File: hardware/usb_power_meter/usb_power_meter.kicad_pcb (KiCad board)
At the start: 4 copper layers, 37.5 x 39.1 mm, 37 parts, among them J1 Conn_ARM_JTAG_SWD_10, J2 917-P81A202ES60201, J4 USB_A, Q1 2N7002, Q2 IRML6401, U1 nRF52833-QDxx, U2 INA226, X1 32Mhz crystal, X2 32.768kHz crystal

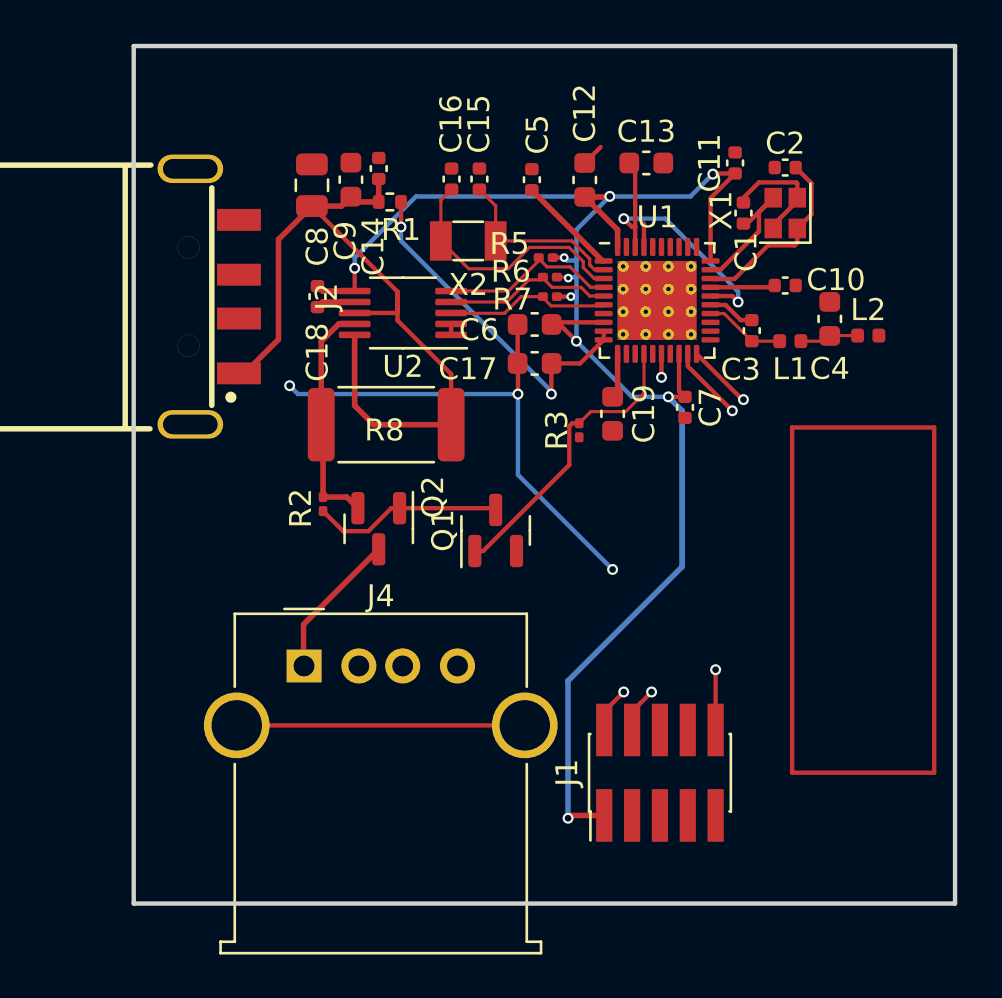
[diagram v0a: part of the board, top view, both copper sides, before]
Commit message: Add an USB socket
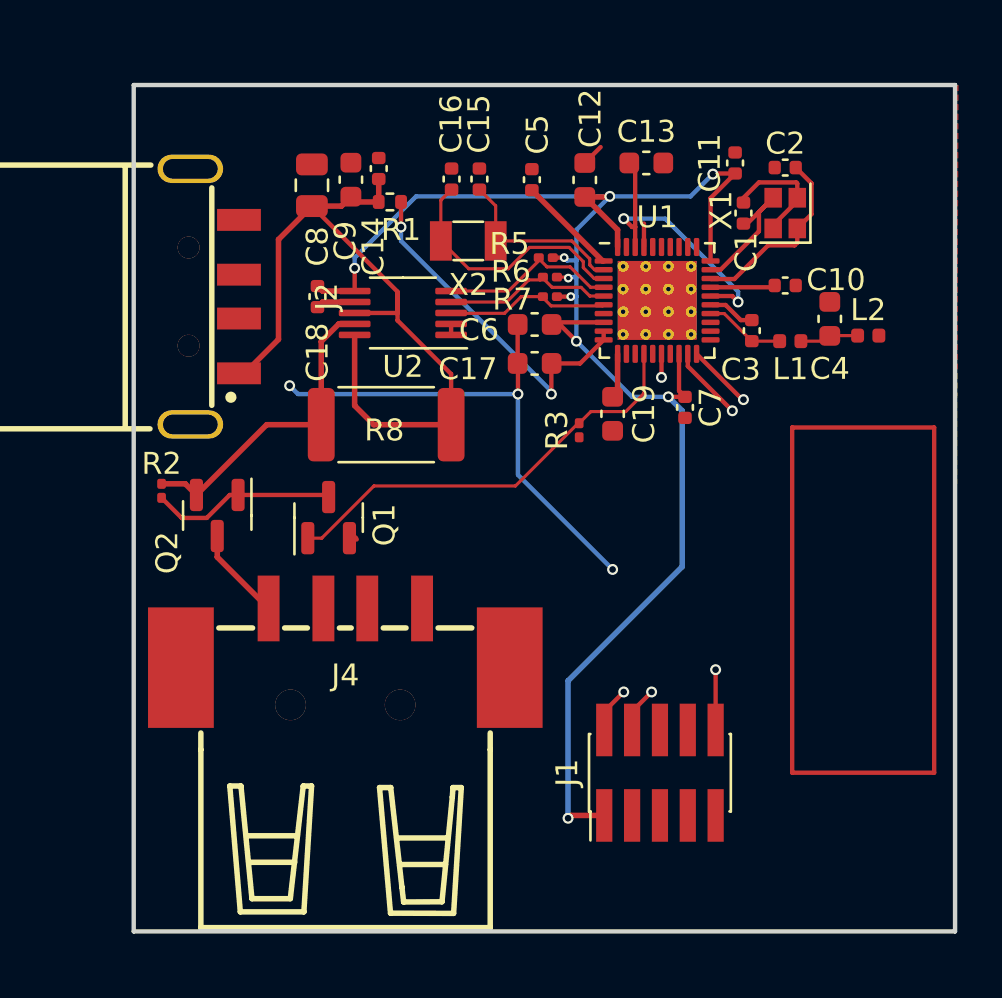
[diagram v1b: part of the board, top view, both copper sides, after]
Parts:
- J4: value USB_A -> A/F LCPTrue color1.2pillar_C42605; footprint Connector_USB:USB_A_Molex_67643_Horizontal -> easyeda2kicad:USB-A-SMD_USB-M-32
- moved Q1 7.64 mm to (119.1, 112.7)
- moved Q2 7.39 mm to (114.0, 112.6)
- moved R2 7.39 mm to (111.5, 111.5)
- moved J4 2.27 mm to (119.9, 118.2)
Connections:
- J4 pad 1: Net-(J4-VBUS) -> GND
- J4 pad 4: GND -> Net-(J4-VCC)
- Q2 pad 3: Net-(J4-VBUS) -> Net-(J4-VCC)
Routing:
- net unconnected-(J4-Pad5): track 13.1 -> 0.00 mm
- net Net-(J4-VBUS): track 6.75 -> 0.00 mm
- net /EN_PWR: track 13.5 -> 19.9 mm
- net Net-(J4-VCC): track 0.00 -> 4.27 mm
- net Net-(Q2-S): track 10.8 -> 14.5 mm
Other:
- board size 37.5 x 39.1 mm -> 37.5 x 38.6 mm

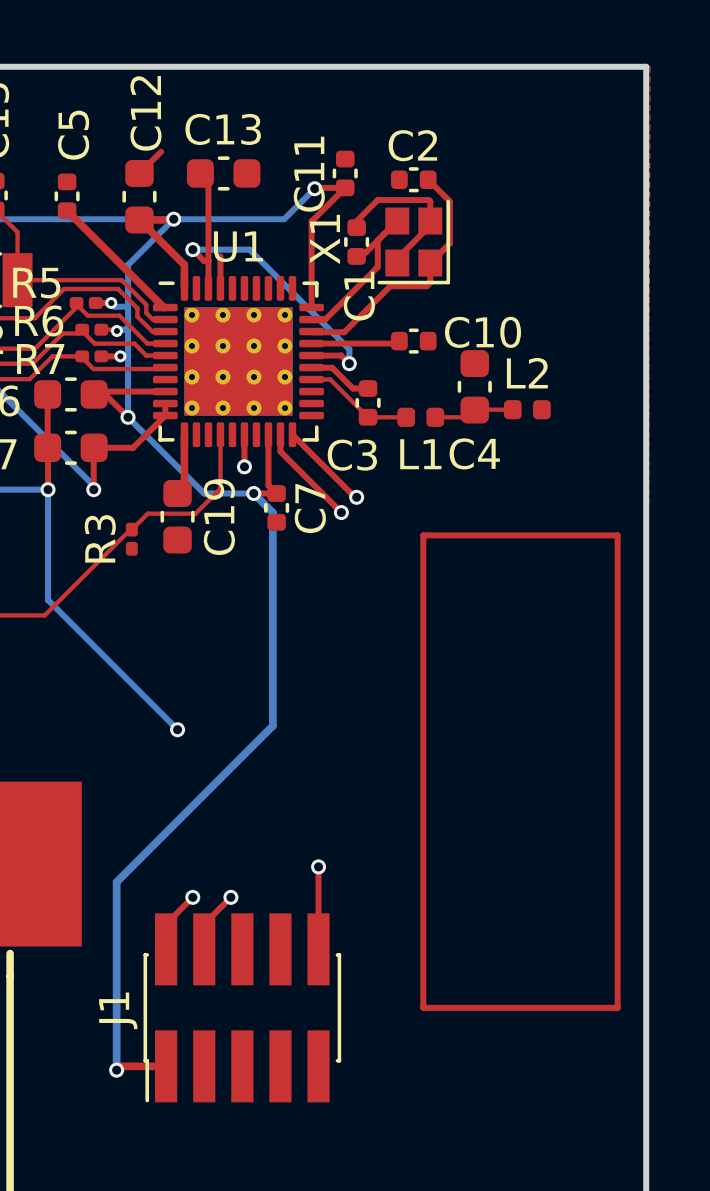
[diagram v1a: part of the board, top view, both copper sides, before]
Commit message: Add the antenna
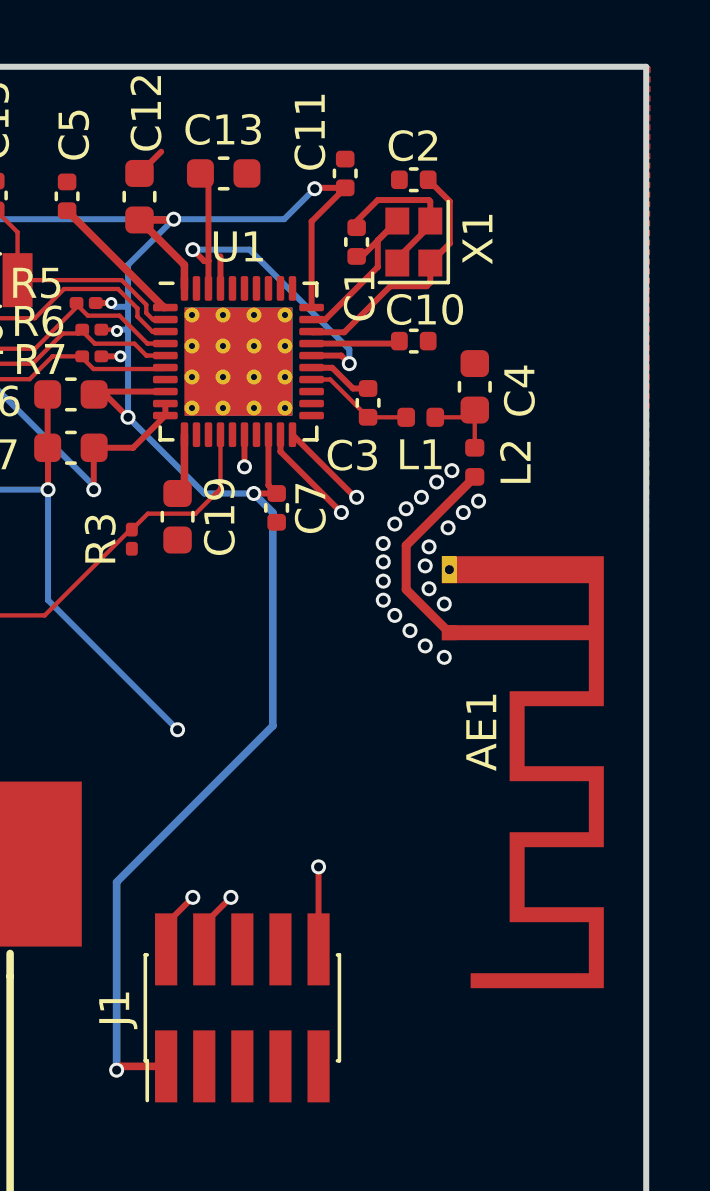
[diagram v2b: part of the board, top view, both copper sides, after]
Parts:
- added AE1: Antenna, RF_Antenna:Texas_SWRA117D_2.4GHz_Right, F.Cu at (141.1, 111.8)
- moved L2 2.48 mm to (142.0, 106.1), turned to -90 degrees
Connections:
- L2 pad 2: unconnected-(L2-Pad2) -> Net-(AE1-A)
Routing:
- net Net-(AE1-A): track 0.00 -> 6.74 mm
- net GND: vias 3 -> 23
- added copper zone on In1.Cu, net GND

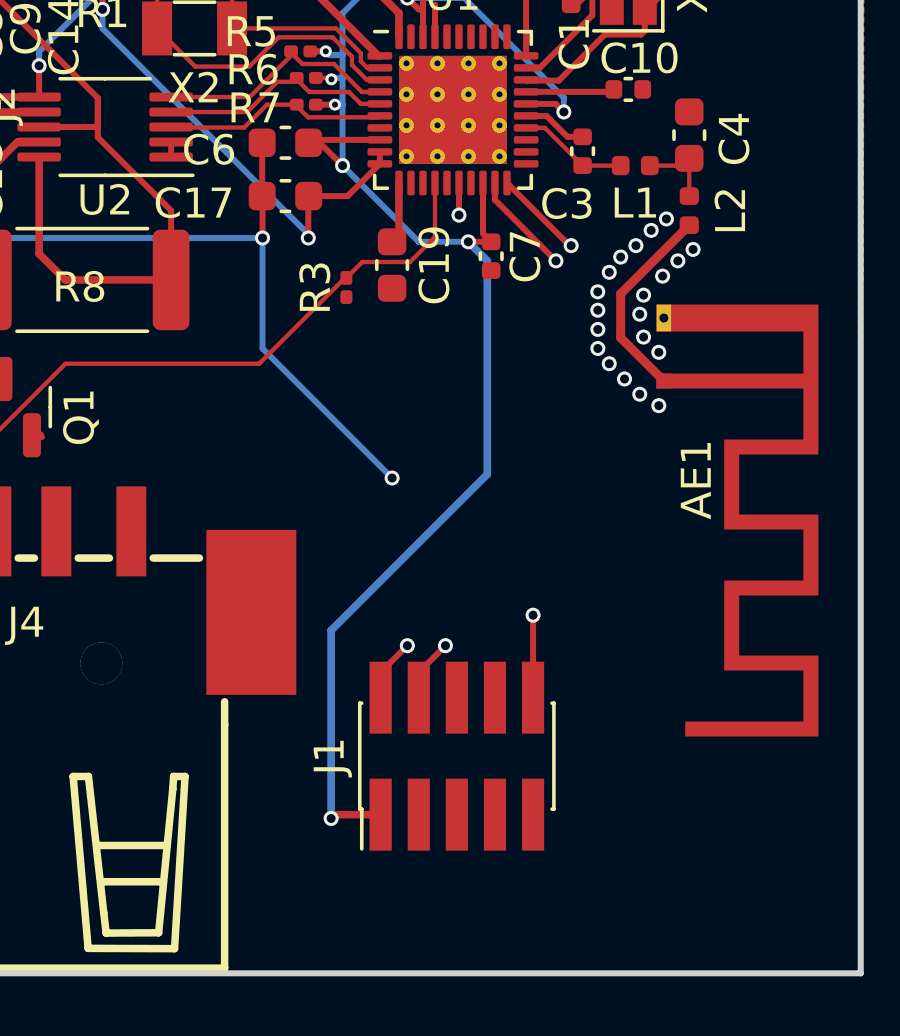
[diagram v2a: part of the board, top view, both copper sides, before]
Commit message: Add and route debugging connectors
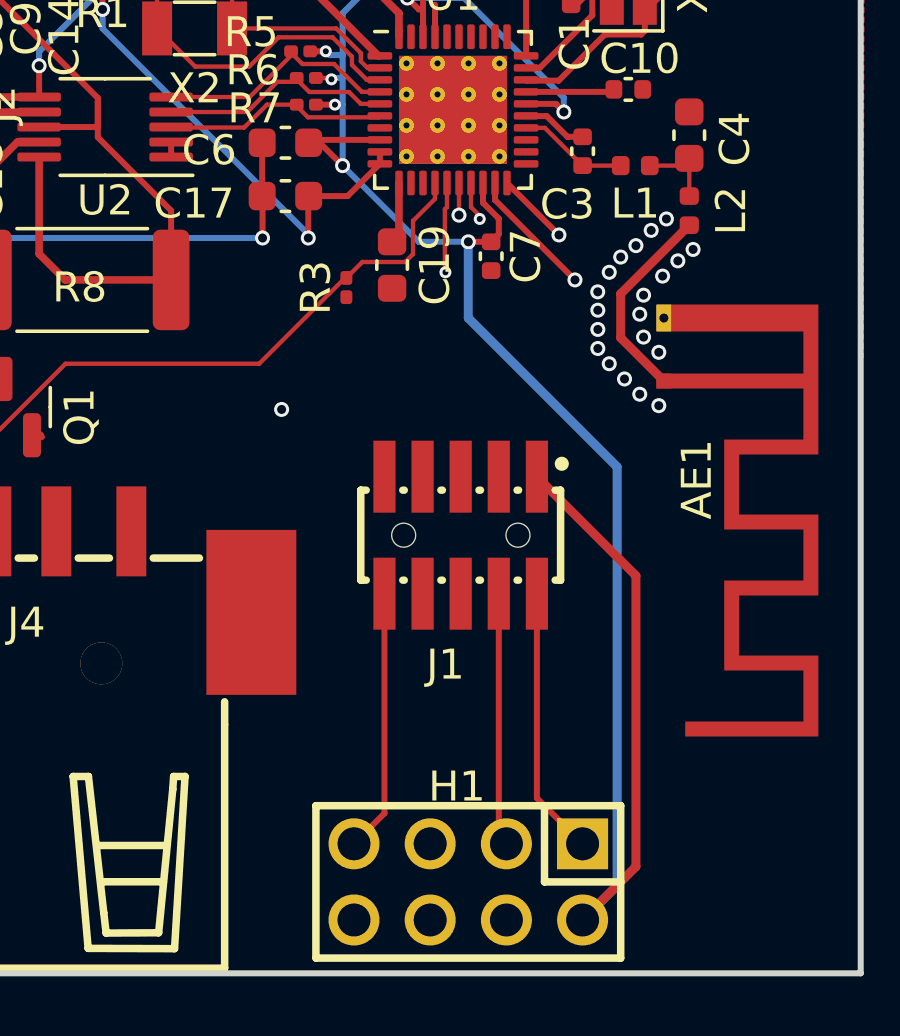
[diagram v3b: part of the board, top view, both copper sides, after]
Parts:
- added H1: DZ254R-22-08-63, easyeda2kicad:HDR-TH_8P-P2.54-V-M-R2-C4-S2.54, F.Cu at (134.6, 128.5)
- J1: value Conn_ARM_JTAG_SWD_10 -> KH-1.27PH180-2X5P-L7.2-SMT; footprint Connector_PinHeader_1.27mm:PinHeader_2x05_P1.27mm_Vertical_SMD -> easyeda2kicad:HDR-SMD_10P-P1.27-V-M-R2-C5-LS5.5
- moved J1 7.37 mm to (134.4, 117.0), turned to 180 degrees
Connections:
- net Net-(J1-SWDCLK/TCK) renamed /SWDCLK
- net Net-(J1-SWDIO/TMS) renamed /SWDIO
- net Net-(J1-~{RESET}) renamed /RST
- AE1 pad 2: GND -> (no net)
- U1 pad 15: unconnected-(U1-P0.17-Pad15) -> /DBG_RX
- U1 pad 17: unconnected-(U1-P0.20-Pad17) -> /DBG_TX
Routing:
- net /DBG_TX: track 0.00 -> 27.9 mm, vias 0 -> 1
- net /DBG_RX: track 0.00 -> 22.3 mm, vias 0 -> 1
- net VDD: track 76.2 -> 95.1 mm, vias 9 -> 8
- net /RST: track 19.2 -> 32.2 mm, vias 2 -> 1
- net GND: track 37.1 -> 27.3 mm
- net /SWDCLK: track 22.3 -> 31.9 mm, vias 2 -> 1
- net /SWDIO: track 22.7 -> 32.2 mm, vias 2 -> 1

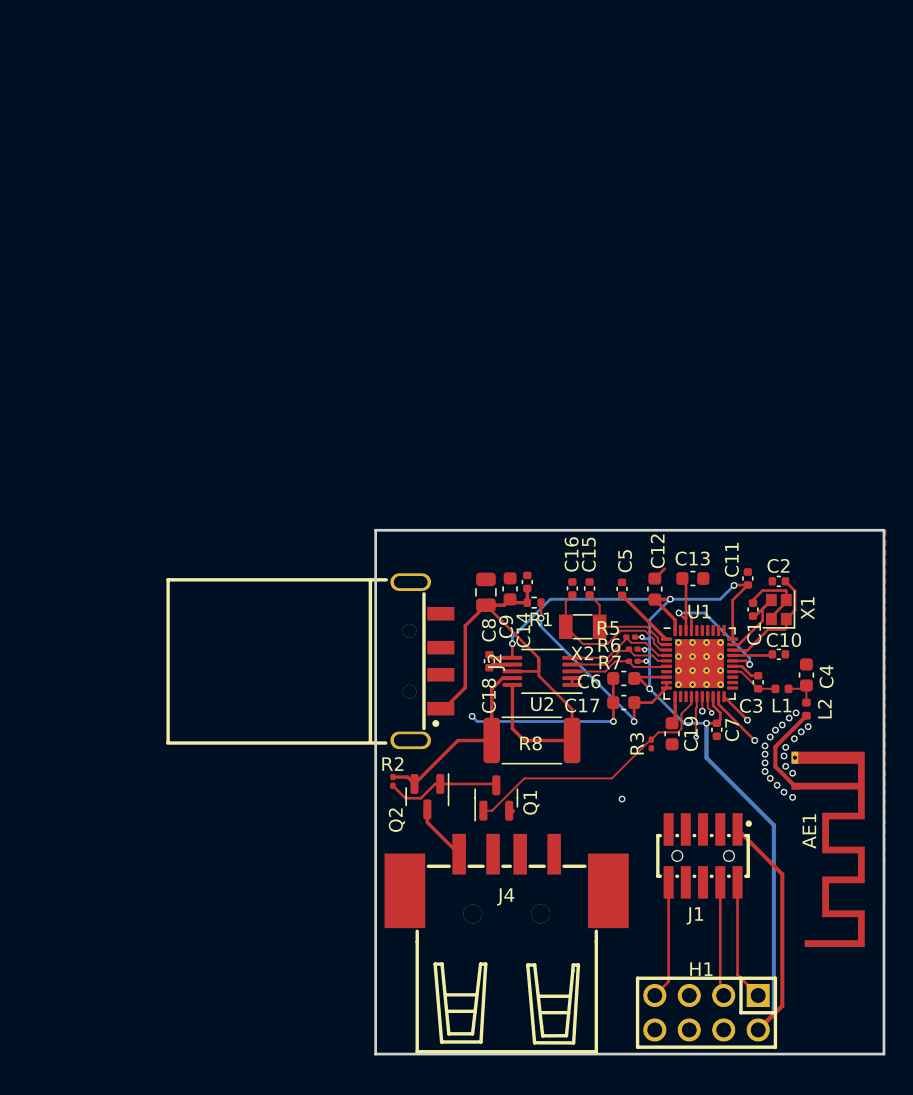
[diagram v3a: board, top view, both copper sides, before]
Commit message: Add mounting holes
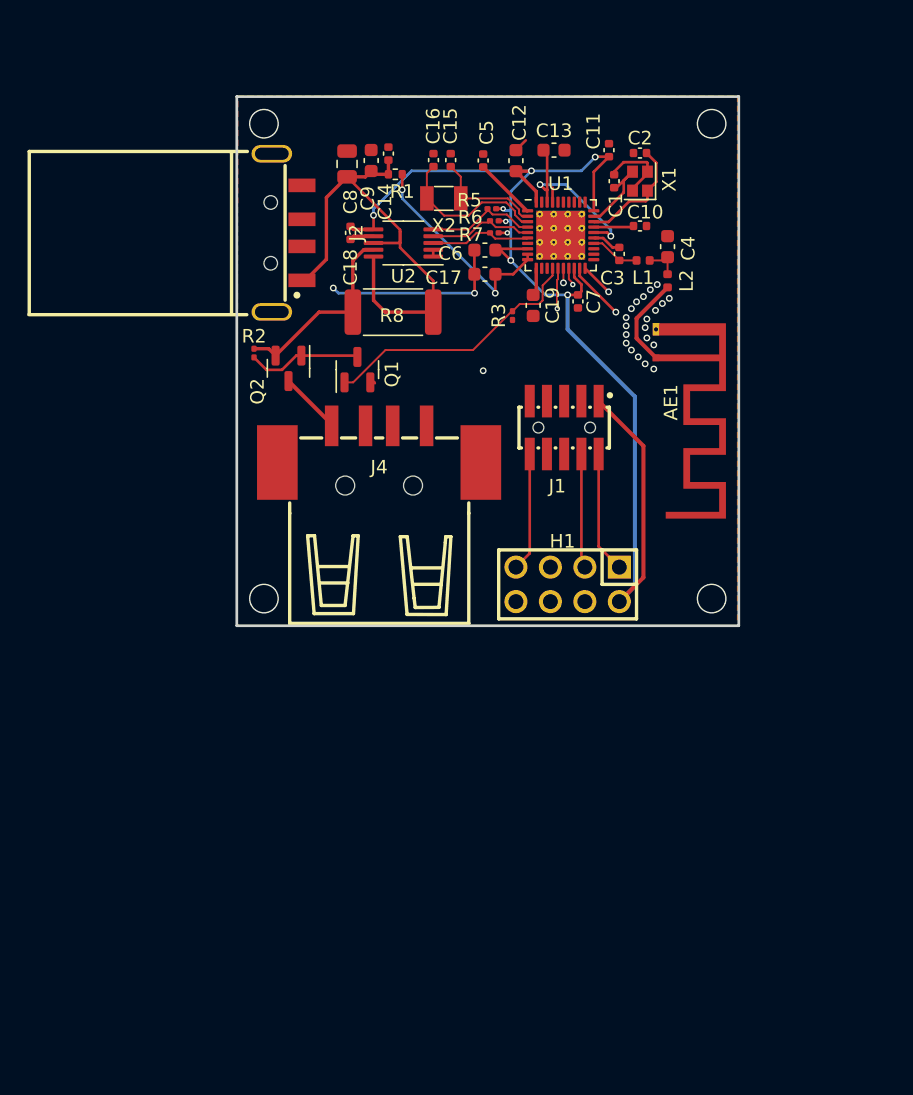
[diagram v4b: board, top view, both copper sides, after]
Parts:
- moved AE1 33.2 mm to (130.9, 80.3)
- moved C1 33.2 mm to (127.8, 67.2)
- moved C10 33.2 mm to (129.7, 70.5)
- moved C11 33.2 mm to (127.4, 64.9)
- moved C12 33.2 mm to (120.6, 65.7)
- moved C14 33.2 mm to (111.2, 65.2)
- moved C15 33.2 mm to (115.8, 65.7)
- moved C17 33.2 mm to (118.3, 74.1)
- moved C2 33.2 mm to (129.7, 65.2)
- moved C3 33.2 mm to (128.2, 72.6)
- moved C6 33.2 mm to (118.3, 72.3)
- moved C7 33.2 mm to (125.1, 76.1)
- moved C8 33.2 mm to (108.1, 66.0)
- moved H1 33.2 mm to (124.4, 97.0)
- moved J1 33.2 mm to (124.1, 85.4)
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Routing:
- net GND: vias 23 -> 26
- net (no net): vias 0 -> 1
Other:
- board size 37.5 x 38.6 mm -> 37 x 39 mm
